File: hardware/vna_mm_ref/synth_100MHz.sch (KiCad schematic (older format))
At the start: 25 parts

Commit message: added regulator to vna mm ref board
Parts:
- added R?: TBD, symbol Device:R_Small
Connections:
- net 10MHZ_IN: now also R?.1
- net GND: now also R?.2
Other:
- note added: "MATCH INPUT IMPEDANCE\n3600 OHM ||4 pF"
- note added: "VCOIN input region is 5 dBm to -15 dBm"
- note removed: "TODO: CHECK INPUT IMPEDANCE"
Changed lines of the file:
@@
 P 3700 4400
 AR Path="/5DC27495" Ref="#PWR?"  Part="1"
-AR Path="/5DC1A65E/5DC27495" Ref="#PWR?"  Part="1"
-F 0 "#PWR?" H 3700 4150 50  0001 C CNN
+AR Path="/5DC1A65E/5DC27495" Ref="#PWR0117"  Part="1"
+F 0 "#PWR0117" H 3700 4150 50  0001 C CNN
 F 1 "GND" H 3705 4227 50  0000 C CNN
 F 2 "" H 3700 4400 50  0001 C CNN
@@
 P 7050 4000
 AR Path="/5DC274A2" Ref="#PWR?"  Part="1"
-AR Path="/5DC1A65E/5DC274A2" Ref="#PWR?"  Part="1"
-F 0 "#PWR?" H 7050 3750 50  0001 C CNN
+AR Path="/5DC1A65E/5DC274A2" Ref="#PWR0118"  Part="1"
+F 0 "#PWR0118" H 7050 3750 50  0001 C CNN
 F 1 "GND" H 7055 3827 50  0000 C CNN
 F 2 "" H 7050 4000 50  0001 C CNN
@@
 P 4900 4000
 AR Path="/5DC274BB" Ref="#PWR?"  Part="1"
-AR Path="/5DC1A65E/5DC274BB" Ref="#PWR?"  Part="1"
-F 0 "#PWR?" H 4900 3750 50  0001 C CNN
+AR Path="/5DC1A65E/5DC274BB" Ref="#PWR0119"  Part="1"
+F 0 "#PWR0119" H 4900 3750 50  0001 C CNN
 F 1 "GND" H 4905 3827 50  0000 C CNN
 F 2 "" H 4900 4000 50  0001 C CNN
@@
 P 5400 4300
 AR Path="/5DC274C8" Ref="#PWR?"  Part="1"
-AR Path="/5DC1A65E/5DC274C8" Ref="#PWR?"  Part="1"
-F 0 "#PWR?" H 5400 4050 50  0001 C CNN
+AR Path="/5DC1A65E/5DC274C8" Ref="#PWR0120"  Part="1"
+F 0 "#PWR0120" H 5400 4050 50  0001 C CNN
 F 1 "GND" H 5405 4127 50  0000 C CNN
 F 2 "" H 5400 4300 50  0001 C CNN
@@
 P 6200 4000
 AR Path="/5DC274E8" Ref="#PWR?"  Part="1"
-AR Path="/5DC1A65E/5DC274E8" Ref="#PWR?"  Part="1"
-F 0 "#PWR?" H 6200 3750 50  0001 C CNN
+AR Path="/5DC1A65E/5DC274E8" Ref="#PWR0121"  Part="1"
+F 0 "#PWR0121" H 6200 3750 50  0001 C CNN
 F 1 "GND" H 6205 3827 50  0000 C CNN
 F 2 "" H 6200 4000 50  0001 C CNN
@@
 P 3700 2050
 AR Path="/5DC274F4" Ref="#PWR?"  Part="1"
-AR Path="/5DC1A65E/5DC274F4" Ref="#PWR?"  Part="1"
-F 0 "#PWR?" H 3700 1900 50  0001 C CNN
+AR Path="/5DC1A65E/5DC274F4" Ref="#PWR0122"  Part="1"
+F 0 "#PWR0122" H 3700 1900 50  0001 C CNN
 F 1 "+3V3" H 3715 2223 50  0000 C CNN
 F 2 "" H 3700 2050 50  0001 C CNN
@@
 P 5100 2950
 AR Path="/5DC27504" Ref="#PWR?"  Part="1"
-AR Path="/5DC1A65E/5DC27504" Ref="#PWR?"  Part="1"
-F 0 "#PWR?" H 5100 2700 50  0001 C CNN
+AR Path="/5DC1A65E/5DC27504" Ref="#PWR0123"  Part="1"
+F 0 "#PWR0123" H 5100 2700 50  0001 C CNN
 F 1 "GND" H 5105 2777 50  0000 C CNN
 F 2 "" H 5100 2950 50  0001 C CNN
@@
 P 4600 2950
 AR Path="/5DC2750D" Ref="#PWR?"  Part="1"
-AR Path="/5DC1A65E/5DC2750D" Ref="#PWR?"  Part="1"
-F 0 "#PWR?" H 4600 2700 50  0001 C CNN
+AR Path="/5DC1A65E/5DC2750D" Ref="#PWR0124"  Part="1"
+F 0 "#PWR0124" H 4600 2700 50  0001 C CNN
 F 1 "GND" H 4605 2777 50  0000 C CNN
 F 2 "" H 4600 2950 50  0001 C CNN
@@
 P 4100 2950
 AR Path="/5DC27514" Ref="#PWR?"  Part="1"
-AR Path="/5DC1A65E/5DC27514" Ref="#PWR?"  Part="1"
-F 0 "#PWR?" H 4100 2700 50  0001 C CNN
+AR Path="/5DC1A65E/5DC27514" Ref="#PWR0125"  Part="1"
+F 0 "#PWR0125" H 4100 2700 50  0001 C CNN
 F 1 "GND" H 4105 2777 50  0000 C CNN
 F 2 "" H 4100 2950 50  0001 C CNN
@@
 P 7050 2150
 AR Path="/5DC27534" Ref="#PWR?"  Part="1"
-AR Path="/5DC1A65E/5DC27534" Ref="#PWR?"  Part="1"
-F 0 "#PWR?" H 7050 2000 50  0001 C CNN
+AR Path="/5DC1A65E/5DC27534" Ref="#PWR0126"  Part="1"
+F 0 "#PWR0126" H 7050 2000 50  0001 C CNN
 F 1 "+3V3" H 7065 2323 50  0000 C CNN
 F 2 "" H 7050 2150 50  0001 C CNN
@@
 P 8450 3050
 AR Path="/5DC27544" Ref="#PWR?"  Part="1"
-AR Path="/5DC1A65E/5DC27544" Ref="#PWR?"  Part="1"
-F 0 "#PWR?" H 8450 2800 50  0001 C CNN
+AR Path="/5DC1A65E/5DC27544" Ref="#PWR0127"  Part="1"
+F 0 "#PWR0127" H 8450 2800 50  0001 C CNN
 F 1 "GND" H 8455 2877 50  0000 C CNN
 F 2 "" H 8450 3050 50  0001 C CNN
@@
 P 7950 3050
 AR Path="/5DC2754D" Ref="#PWR?"  Part="1"
-AR Path="/5DC1A65E/5DC2754D" Ref="#PWR?"  Part="1"
-F 0 "#PWR?" H 7950 2800 50  0001 C CNN
+AR Path="/5DC1A65E/5DC2754D" Ref="#PWR0128"  Part="1"
+F 0 "#PWR0128" H 7950 2800 50  0001 C CNN
 F 1 "GND" H 7955 2877 50  0000 C CNN
 F 2 "" H 7950 3050 50  0001 C CNN
@@
 P 7450 3050
 AR Path="/5DC27554" Ref="#PWR?"  Part="1"
-AR Path="/5DC1A65E/5DC27554" Ref="#PWR?"  Part="1"
-F 0 "#PWR?" H 7450 2800 50  0001 C CNN
+AR Path="/5DC1A65E/5DC27554" Ref="#PWR0129"  Part="1"
+F 0 "#PWR0129" H 7450 2800 50  0001 C CNN
 F 1 "GND" H 7455 2877 50  0000 C CNN
 F 2 "" H 7450 3050 50  0001 C CNN
@@
 P 7250 5100
 AR Path="/5DC275AC" Ref="#PWR?"  Part="1"
-AR Path="/5DC1A65E/5DC275AC" Ref="#PWR?"  Part="1"
-F 0 "#PWR?" H 7250 4850 50  0001 C CNN
+AR Path="/5DC1A65E/5DC275AC" Ref="#PWR0130"  Part="1"
+F 0 "#PWR0130" H 7250 4850 50  0001 C CNN
 F 1 "GND" H 7255 4927 50  0000 C CNN
 F 2 "" H 7250 5100 50  0001 C CNN
@@
 P 7800 5100
 AR Path="/5DC275B2" Ref="#PWR?"  Part="1"
-AR Path="/5DC1A65E/5DC275B2" Ref="#PWR?"  Part="1"
-F 0 "#PWR?" H 7800 4850 50  0001 C CNN
+AR Path="/5DC1A65E/5DC275B2" Ref="#PWR0131"  Part="1"
+F 0 "#PWR0131" H 7800 4850 50  0001 C CNN
 F 1 "GND" H 7805 4927 50  0000 C CNN
 F 2 "" H 7800 5100 50  0001 C CNN
@@
 P 4350 4600
 AR Path="/5DC275C7" Ref="#PWR?"  Part="1"
-AR Path="/5DC1A65E/5DC275C7" Ref="#PWR?"  Part="1"
-F 0 "#PWR?" H 4350 4350 50  0001 C CNN
+AR Path="/5DC1A65E/5DC275C7" Ref="#PWR0132"  Part="1"
+F 0 "#PWR0132" H 4350 4350 50  0001 C CNN
 F 1 "GND" H 4355 4427 50  0000 C CNN
 F 2 "" H 4350 4600 50  0001 C CNN
@@
 Wire Wire Line
 	8800 3600 8600 3600
-Text HLabel 2350 3600 0    50   Input ~ 0
+Text HLabel 1700 3600 0    50   Input ~ 0
 10MHZ_IN
-Wire Wire Line
-	3150 3600 2350 3600
-Text Notes 1750 3450 0    50   ~ 0
-TODO: CHECK INPUT IMPEDANCE
+Text Notes 1850 3500 0    50   ~ 0
+MATCH INPUT IMPEDANCE\n3600 OHM ||4 pF
 $Comp
 L vna_mm:HMC1031 U?
@@
 Wire Wire Line
 	4250 3800 4700 3800
+Wire Wire Line
+	1700 3600 1900 3600
+$Comp
+L Device:R_Small R?
+U 1 1 5DB93EC3
+P 1900 4000
+AR Path="/5DB93EC3" Ref="R?"  Part="1"
+AR Path="/5DC1A65E/5DB93EC3" Ref="R?"  Part="1"
+F 0 "R?" H 1959 4046 50  0000 L CNN
+F 1 "TBD" H 1959 3955 50  0000 L CNN
+F 2 "" H 1900 4000 50  0001 C CNN
+F 3 "~" H 1900 4000 50  0001 C CNN
+	1    1900 4000
+	1    0    0    -1
+$EndComp
+$Comp
+L power:GND #PWR?
+U 1 1 5DB944B7
+P 1900 4400
+AR Path="/5DB944B7" Ref="#PWR?"  Part="1"
+AR Path="/5DC1A65E/5DB944B7" Ref="#PWR0133"  Part="1"
+F 0 "#PWR0133" H 1900 4150 50  0001 C CNN
+F 1 "GND" H 1905 4227 50  0000 C CNN
+F 2 "" H 1900 4400 50  0001 C CNN
+F 3 "" H 1900 4400 50  0001 C CNN
+	1    1900 4400
+	1    0    0    -1
+$EndComp
+Wire Wire Line
+	1900 4400 1900 4100
+Wire Wire Line
+	1900 3900 1900 3600
+Connection ~ 1900 3600
+Wire Wire Line
+	1900 3600 3150 3600
+Text Notes 5050 4750 0    50   ~ 0
+VCOIN input region is 5 dBm to -15 dBm
 $EndSCHEMATC

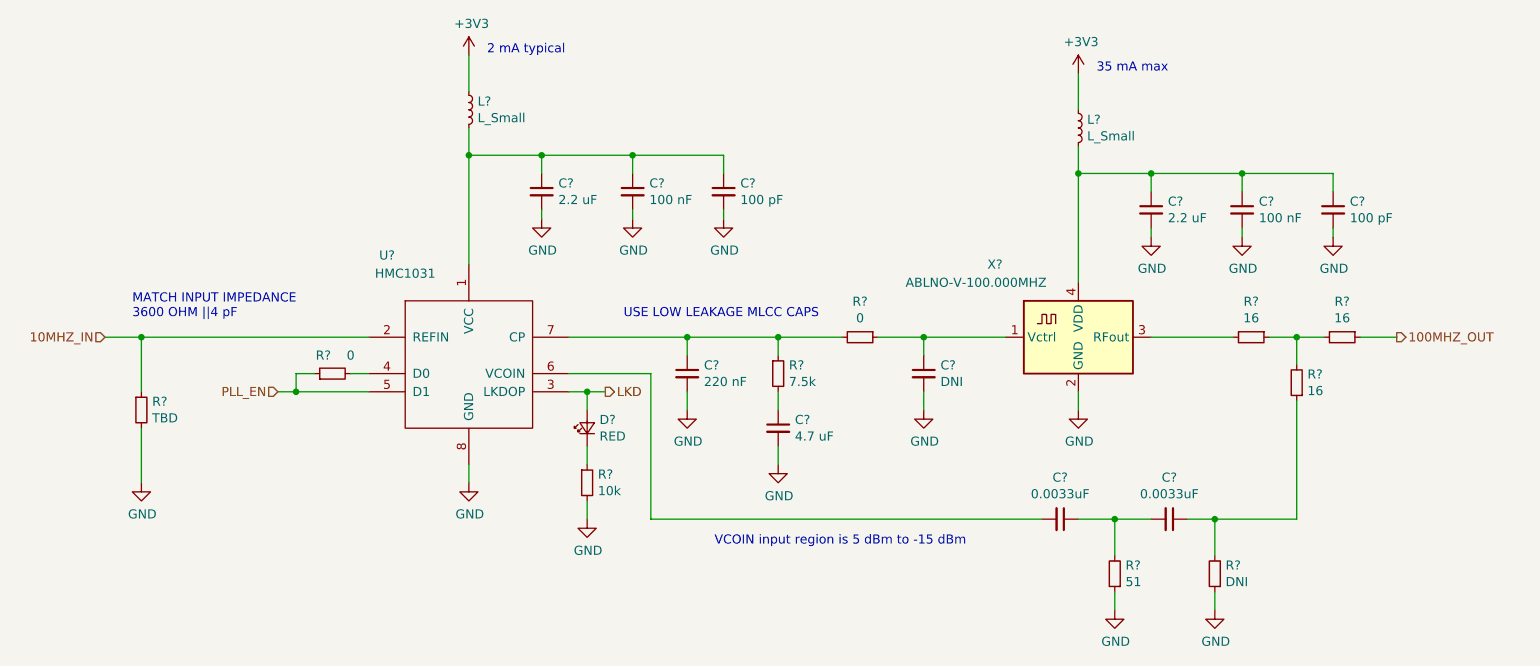
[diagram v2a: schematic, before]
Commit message: added protection to digital inputs
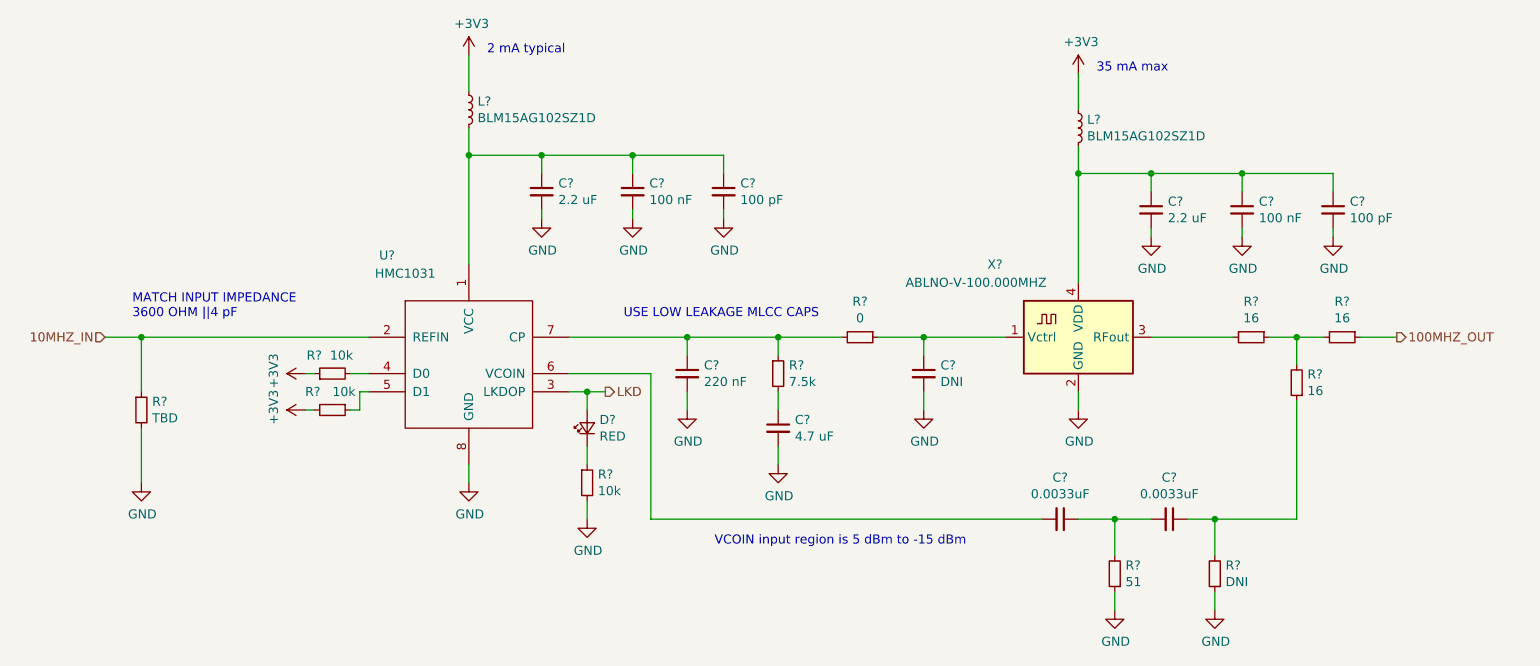
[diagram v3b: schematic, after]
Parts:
- added R?: 10k, symbol Device:R_Small
- L? (x2): value L_Small -> BLM15AG102SZ1D
- R?: value 0 -> 10k
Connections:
- net +3V3: now also R?.1, R?.2
- net PLL_EN: no longer names the net of U?.5 (D1)
- net PLL_EN: now also R?.1; no longer R?.1
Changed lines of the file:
@@
 AR Path="/5DC274A9" Ref="R?"  Part="1"
 AR Path="/5DC1A65E/5DC274A9" Ref="R?"  Part="1"
-F 0 "R?" V 3050 3850 50  0000 C CNN
-F 1 "0" V 3050 3700 50  0000 C CNN
+F 0 "R?" V 3050 3900 50  0000 C CNN
+F 1 "10k" V 3050 3750 50  0000 C CNN
 F 2 "" H 2950 3800 50  0001 C CNN
 F 3 "~" H 2950 3800 50  0001 C CNN
@@
 AR Path="/5DC1A65E/5DC2751A" Ref="L?"  Part="1"
 F 0 "L?" H 3748 2396 50  0000 L CNN
-F 1 "L_Small" H 3748 2305 50  0000 L CNN
+F 1 "BLM15AG102SZ1D" H 3748 2305 50  0000 L CNN
 F 2 "" H 3700 2350 50  0001 C CNN
 F 3 "~" H 3700 2350 50  0001 C CNN
@@
 AR Path="/5DC1A65E/5DC2755A" Ref="L?"  Part="1"
 F 0 "L?" H 7098 2496 50  0000 L CNN
-F 1 "L_Small" H 7098 2405 50  0000 L CNN
+F 1 "BLM15AG102SZ1D" H 7098 2405 50  0000 L CNN
 F 2 "" H 7050 2450 50  0001 C CNN
 F 3 "~" H 7050 2450 50  0001 C CNN
@@
 Wire Wire Line
 	3050 3800 3150 3800
-Wire Wire Line
-	3150 3900 2750 3900
-Wire Wire Line
-	2750 3900 2750 3800
-Wire Wire Line
-	2750 3800 2850 3800
-Wire Wire Line
-	2650 3900 2750 3900
-Connection ~ 2750 3900
 Text HLabel 8800 3600 2    50   Output ~ 0
 100MHZ_OUT
@@
 	1    0    0    -1
 $EndComp
-Text HLabel 2650 3900 0    50   Input ~ 0
-PLL_EN
 Text HLabel 4450 3900 2    50   Output ~ 0
 LKD
@@
 Text Notes 5050 4750 0    50   ~ 0
 VCOIN input region is 5 dBm to -15 dBm
+$Comp
+L power:+3V3 #PWR?
+U 1 1 5DED131B
+P 2800 4000
+AR Path="/5DED131B" Ref="#PWR?"  Part="1"
+AR Path="/5DC1A65E/5DED131B" Ref="#PWR?"  Part="1"
+F 0 "#PWR?" H 2800 3850 50  0001 C CNN
+F 1 "+3V3" H 2815 4173 50  0000 C CNN
+F 2 "" H 2800 4000 50  0001 C CNN
+F 3 "" H 2800 4000 50  0001 C CNN
+	1    2800 4000
+	0    -1   -1   0
+$EndComp
+$Comp
+L Device:R_Small R?
+U 1 1 5DED19AB
+P 2950 4000
+AR Path="/5DED19AB" Ref="R?"  Part="1"
+AR Path="/5DC1A65E/5DED19AB" Ref="R?"  Part="1"
+F 0 "R?" V 2850 3850 50  0000 L CNN
+F 1 "10k" V 2850 4000 50  0000 L CNN
+F 2 "" H 2950 4000 50  0001 C CNN
+F 3 "~" H 2950 4000 50  0001 C CNN
+	1    2950 4000
+	0    1    1    0
+$EndComp
+Wire Wire Line
+	2850 4000 2800 4000
+$Comp
+L power:+3V3 #PWR?
+U 1 1 5DED581B
+P 2800 3800
+AR Path="/5DED581B" Ref="#PWR?"  Part="1"
+AR Path="/5DC1A65E/5DED581B" Ref="#PWR?"  Part="1"
+F 0 "#PWR?" H 2800 3650 50  0001 C CNN
+F 1 "+3V3" H 2815 3973 50  0000 C CNN
+F 2 "" H 2800 3800 50  0001 C CNN
+F 3 "" H 2800 3800 50  0001 C CNN
+	1    2800 3800
+	0    -1   -1   0
+$EndComp
+Wire Wire Line
+	2800 3800 2850 3800
+Wire Wire Line
+	3050 4000 3100 4000
+Wire Wire Line
+	3100 4000 3100 3900
+Wire Wire Line
+	3100 3900 3150 3900
 $EndSCHEMATC

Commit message: footprint assignment on reference board
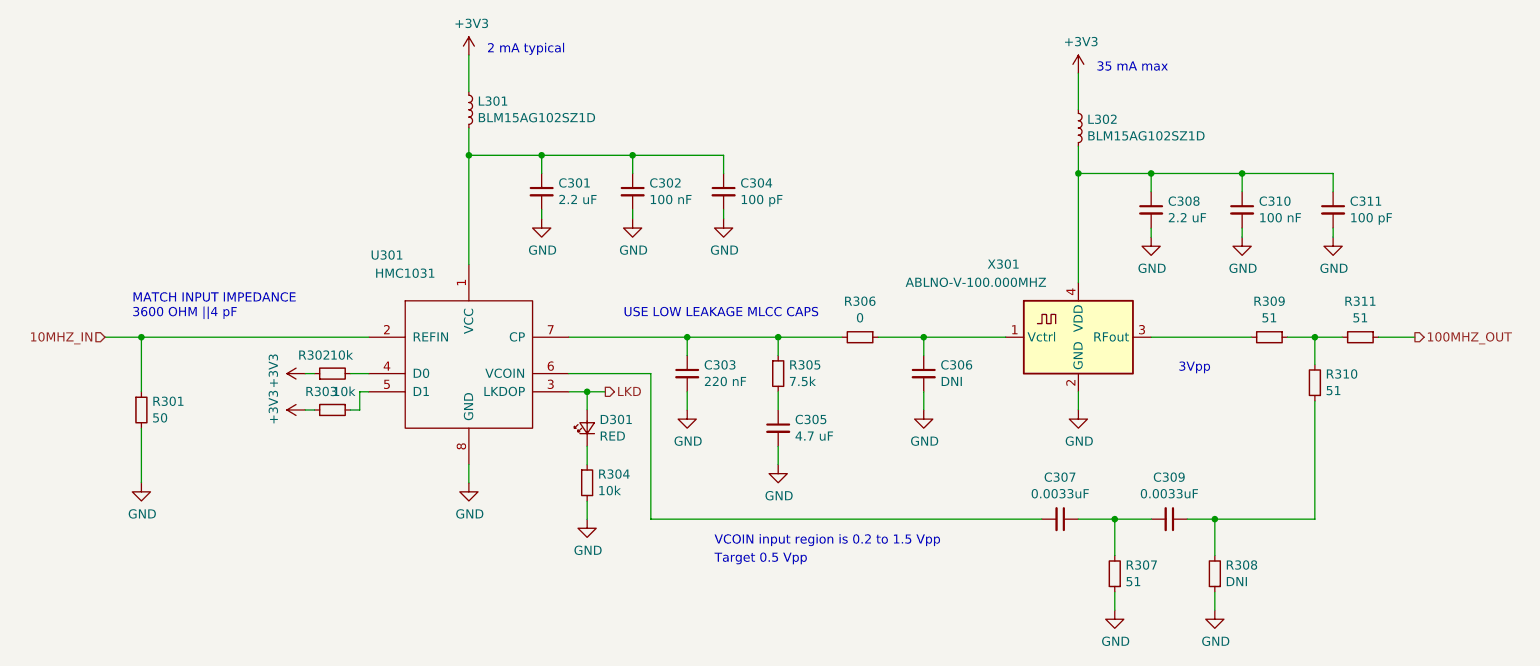
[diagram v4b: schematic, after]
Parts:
- C301, C305, C308: renamed from C?; footprint (none) -> Capacitor_SMD:C_0603_1608Metric
- C302, C303, C304, C306, C307, C309, C310, C311: renamed from C?; footprint (none) -> Capacitor_SMD:C_0402_1005Metric
- D301: renamed from D?; footprint (none) -> LED_SMD:LED_0603_1608Metric
- L301, L302: renamed from L?; footprint (none) -> Inductor_SMD:L_0402_1005Metric
- R301: renamed from R?; value TBD -> 50; footprint (none) -> Resistor_SMD:R_0402_1005Metric
- R302, R303, R304, R305, R306, R307, R308: renamed from R?; footprint (none) -> Resistor_SMD:R_0402_1005Metric
- R309, R310, R311: renamed from R?; value 16 -> 51; footprint (none) -> Resistor_SMD:R_0402_1005Metric
- gave numbers to parts that had none: 2
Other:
- note added: "3Vpp"
- note added: "Target 0.5 Vpp"
- note added: "VCOIN input region is 0.2 to 1.5 Vpp"
- note removed: "VCOIN input region is 5 dBm to -15 dBm"
- moved on the sheet: R309, R310, R311
